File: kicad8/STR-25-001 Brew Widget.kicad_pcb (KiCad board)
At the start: 2 copper layers, 0 parts

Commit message: Started PCB Layout
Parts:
- added BT1: 18650, Battery:BatteryHolder_Keystone_1042_1x18650, B.Cu at (144.5, 114.9)
- added C1: 100nF, JLCPCB-Kicad-Footprints:C_0402, F.Cu at (153.3, 83.5)
- added C10: 100nF, JLCPCB-Kicad-Footprints:C_0402, F.Cu at (144.5, 117.8)
- added C11: 100nF, JLCPCB-Kicad-Footprints:C_0402, F.Cu at (147.0, 116.0)
- added C12: 10uF, JLCPCB-Kicad-Footprints:C_0402, F.Cu at (141.1, 107.0)
- added C13: 1uF, JLCPCB-Kicad-Footprints:C_0402, F.Cu at (118.0, 114.5)
- added C14: 100nF, JLCPCB-Kicad-Footprints:C_0402, F.Cu at (149.4, 108.8)
- added C15: 100nF, JLCPCB-Kicad-Footprints:C_0402, F.Cu at (152.4, 147.5)
- added C2: 4.7uF, JLCPCB-Kicad-Footprints:C_0402, F.Cu at (139.8, 82.5)
- added C3: 100nF, JLCPCB-Kicad-Footprints:C_0402, F.Cu at (139.8, 83.5)
- added C4: 100nF, JLCPCB-Kicad-Footprints:C_0402, F.Cu at (140.2, 77.8)
- added C5: 10uF, JLCPCB-Kicad-Footprints:C_0402, F.Cu at (139.2, 77.8)
- added C6: 10uF, JLCPCB-Kicad-Footprints:C_0402, F.Cu at (143.5, 117.8)
- added C7: 4.7uF, JLCPCB-Kicad-Footprints:C_0402, F.Cu at (120.4, 121.2)
- added C8: 4.7uF, JLCPCB-Kicad-Footprints:C_0402, F.Cu at (145.9, 105.8)
- added C9: 10pF, JLCPCB-Kicad-Footprints:C_0402, F.Cu at (118.0, 112.7)
- added D1: B16WS, JLCPCB-Kicad-Footprints:D_SOD-323, F.Cu at (113.7, 113.0)
- added D2: Red, LED_SMD:LED_0603_1608Metric, F.Cu at (141.7, 101.0)
- added D3: Green, LED_SMD:LED_0603_1608Metric, F.Cu at (144.0, 101.0)
- added D4: B16WS, JLCPCB-Kicad-Footprints:D_SOD-323, F.Cu at (137.5, 120.2)
- added H1: ~, JLCPCB-Kicad-Footprints:Hole_Tooling_JLCPCB, F.Cu at (178.3, 116.8)
- added H2: ~, JLCPCB-Kicad-Footprints:Hole_Tooling_JLCPCB, F.Cu at (178.3, 119.8)
- added H3: ~, JLCPCB-Kicad-Footprints:Hole_Tooling_JLCPCB, F.Cu at (178.3, 122.8)
- added J1: USB_B_Micro, STR-USB:USB_Micro-B_C319160, F.Cu at (136.2, 73.6)
- added L1: 10uH,600mA, Inductor_SMD:L_Wuerth_WE-GF-1210, F.Cu at (137.2, 117.0)
- added PN1: ~, JLCPCB-Kicad-Footprints:Part_Num_JLCPCB, F.Cu at (181.5, 114.5)
- added Q1: IRLML6401, Package_TO_SOT_SMD:SOT-23, F.Cu at (137.1, 108.7)
- added Q2: FS8205A, Package_TO_SOT_SMD:SOT-23-6, F.Cu at (145.5, 148.0)
- added R1: 10kΩ, JLCPCB-Kicad-Footprints:R_0402, F.Cu at (139.8, 79.2)
- added R10: 2kΩ, JLCPCB-Kicad-Footprints:R_0402, F.Cu at (145.9, 103.9)
- added R11: 200kΩ, JLCPCB-Kicad-Footprints:R_0402, F.Cu at (118.0, 120.1)
- added R12: 120kΩ, JLCPCB-Kicad-Footprints:R_0402, F.Cu at (118.0, 121.9)
- added R13: 4.7kΩ, JLCPCB-Kicad-Footprints:R_0402, F.Cu at (144.3, 158.2)
- added R14: 100Ω, JLCPCB-Kicad-Footprints:R_0402, F.Cu at (153.4, 147.5)
- added R15: 0Ω, JLCPCB-Kicad-Footprints:R_0402, F.Cu at (141.9, 148.9)
- added R16: 1kΩ, JLCPCB-Kicad-Footprints:R_0402, F.Cu at (148.7, 150.3)
- added R17: 10kΩ, JLCPCB-Kicad-Footprints:R_0402, F.Cu at (153.0, 110.3)
- added R2: 10kΩ, JLCPCB-Kicad-Footprints:R_0402, F.Cu at (153.3, 84.5)
- added R3: 10kΩ, JLCPCB-Kicad-Footprints:R_0402, F.Cu at (139.8, 81.5)
- added R4: 10kΩ, JLCPCB-Kicad-Footprints:R_0402, F.Cu at (139.8, 84.4)
- added R5: 4.7kΩ, JLCPCB-Kicad-Footprints:R_0402, F.Cu at (143.9, 111.2)
- added R6: 4.7kΩ, JLCPCB-Kicad-Footprints:R_0402, F.Cu at (141.9, 111.2)
- added R7: 10kΩ, JLCPCB-Kicad-Footprints:R_0402, F.Cu at (151.2, 83.5)
- added R8: 100kΩ, JLCPCB-Kicad-Footprints:R_0402, F.Cu at (118.0, 118.2)
- added R9: 2kΩ, JLCPCB-Kicad-Footprints:R_0402, F.Cu at (142.8, 98.7)
- added SW1: SW_MINI, STR-Switch:SW_SMD_SPST_8x3.6, F.Cu at (147.5, 90.2)
- added SW2: SW_MINI, STR-Switch:SW_SMD_SPST_8x3.6, F.Cu at (141.2, 90.2)
- added U1: ESP32-C3-MINI-1-N4, STR-ESP32:ESP32-C3-MINI-1-N4, F.Cu at (148.7, 74.0)
- added U2: TPS61040, JLCPCB-Kicad-Footprints:SOT-23-5_L3.0-W1.7-P0.95-LS2.8-BL, F.Cu at (123.0, 118.5)
- added U3: TP4057, Package_TO_SOT_SMD:TSOT-23-6, F.Cu at (142.8, 104.9)
- added U4: MPU-6500, Sensor_Motion:InvenSense_QFN-24_3x3mm_P0.4mm_NoMask, F.Cu at (144.2, 114.5)
- added U5: DS18B20U, Package_SO:MSOP-8_3x3mm_P0.65mm, F.Cu at (144.5, 160.5)
- added U6: MAX17048, Package_DFN_QFN:TDFN-8-1EP_2x2mm_P0.5mm_EP0.8x1.2mm, F.Cu at (151.5, 108.5)
- added U7: DW01A, Package_TO_SOT_SMD:SOT-23-6, F.Cu at (149.8, 147.9)
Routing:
- net +BATT: track 0.00 -> 93.4 mm, vias 0 -> 4
- net GND: track 0.00 -> 78.8 mm, vias 0 -> 29
- net -BATT: track 0.00 -> 55.4 mm
- net USB_D+: track 0.00 -> 47.9 mm
- net USB_D-: track 0.00 -> 45.6 mm
- net SCA: track 0.00 -> 38.1 mm, vias 0 -> 2
- net VBUS: track 0.00 -> 35.8 mm, vias 0 -> 4
- net SCL: track 0.00 -> 32.7 mm, vias 0 -> 1
- net +3.3V: track 0.00 -> 29.7 mm, vias 0 -> 11
- net /-BATT_NOPROT: track 0.00 -> 22.1 mm, vias 0 -> 3
- net EN: track 0.00 -> 9.87 mm
- net GPIO9: track 0.00 -> 8.95 mm
- net ~{BAT_ALERT}: track 0.00 -> 7.37 mm
- net Net-(U1-IO2): track 0.00 -> 4.95 mm
- net Net-(D3-K): track 0.00 -> 4.93 mm
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- added copper zone on In1.Cu, net +3.3V
- added copper zone on In2.Cu, net GND
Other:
- board outline added: 25 x 94 mm
- copper layers 2 -> 4

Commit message: PCB routed and all 3d models correct, needs final review
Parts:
- removed the C13 at (118.0, 114.5)
- removed H1, H2, H3: ~, JLCPCB-Kicad-Footprints:Hole_Tooling_JLCPCB
- removed the U2 at (123.0, 118.5)
- added C10: 100pF, JLCPCB-Kicad-Footprints:C_0402, F.Cu at (141.8, 116.9)
- added C16: 100pF, JLCPCB-Kicad-Footprints:C_0402, F.Cu at (137.3, 126.5)
- added C17: 1uF, JLCPCB-Kicad-Footprints:C_0402, F.Cu at (137.3, 127.4)
- added C18: 10uF, JLCPCB-Kicad-Footprints:C_0402, F.Cu at (137.3, 128.3)
- added C19: 10uF, JLCPCB-Kicad-Footprints:C_0402, F.Cu at (137.3, 129.2)
- added C8: 10uF, JLCPCB-Kicad-Footprints:C_0402, F.Cu at (141.8, 115.1)
- added C9: 1uF, JLCPCB-Kicad-Footprints:C_0402, F.Cu at (141.8, 116.0)
- added TP1: TestPoint, TestPoint:TestPoint_Pad_D2.0mm, F.Cu at (134.6, 84.0)
- added TP10: TestPoint, TestPoint:TestPoint_Pad_D1.0mm, F.Cu at (133.9, 77.3)
- added TP11: TestPoint, TestPoint:TestPoint_Pad_D1.0mm, F.Cu at (133.9, 79.5)
- added TP2: TestPoint, TestPoint:TestPoint_Pad_D2.0mm, F.Cu at (136.3, 114.0)
- added TP3: TestPoint, TestPoint:TestPoint_Pad_D2.0mm, F.Cu at (136.4, 134.6)
- added TP4: TestPoint, TestPoint:TestPoint_Pad_D2.0mm, F.Cu at (151.8, 142.3)
- added TP5: TestPoint, TestPoint:TestPoint_Pad_D2.0mm, F.Cu at (153.5, 104.3)
- added TP6: TestPoint, TestPoint:TestPoint_Pad_D2.0mm, F.Cu at (141.3, 97.7)
- added TP7: TestPoint, TestPoint:TestPoint_Pad_D2.0mm, F.Cu at (147.3, 97.8)
- added TP8: TestPoint, TestPoint:TestPoint_Pad_D2.0mm, F.Cu at (145.1, 142.2)
- added TP9: TestPoint, TestPoint:TestPoint_Pad_2.5x2.5mm, F.Cu at (151.8, 133.3)
- added U3: MT3608, Package_TO_SOT_SMD:SOT-23-6, F.Cu at (140.3, 119.7)
- C7: value 4.7uF -> 10uF
- D2: value Red -> CHG
- D3: value Green -> STBY
- J1: footprint STR-USB:USB_Micro-B_C319160 -> Connector_USB:USB_Micro-B_Molex_47346-0001
- L1: value 10uH,600mA -> 22uH,540mA; footprint Inductor_SMD:L_Wuerth_WE-GF-1210 -> STR-Passive:IND_LQH3NPZ220MMEL
- R11: value 200kΩ -> 68kΩ
- R12: value 120kΩ -> 15kΩ
- SW1: value SW_MINI -> BOOT
- SW2: value SW_MINI -> RESET
- moved PN1 47.5 mm to (148.5, 80.3)
- moved C13 26.0 mm to (141.4, 124.1), turned to 90 degrees
- moved R11 24.7 mm to (142.4, 124.1), turned to 90 degrees
- moved R12 22.9 mm to (140.9, 122.6), turned to 180 degrees
- moved C7 22.6 mm to (141.8, 114.1), turned to 0 degrees
- moved D1 21.8 mm to (135.2, 109.5), turned to 90 degrees
- moved R8 18.2 mm to (133.7, 109.0), turned to -90 degrees
- moved C15 10.0 mm to (136.5, 98.1)
- moved D3 9.49 mm to (134.6, 102.0), turned to 180 degrees
- moved C11 8.79 mm to (137.6, 103.1)
- moved R9 8.78 mm to (134.2, 97.1)
- moved D2 7.29 mm to (134.5, 99.4), turned to 180 degrees
- moved R5 7.08 mm to (144.6, 104.1)
- moved R6 7.08 mm to (142.6, 104.1)
- moved C12 7.04 mm to (145.2, 110.7)
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- renumbered C8 to C11, C10 to C12, C9 to C13, C11 to C14, C12 to C15, C14 to C20, C15 to C21, R14 to R13, R13 to R14, R17 to R15, R15 to R16, R16 to R17, U3 to U2, U6 to U5, U5 to U6
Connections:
- net Net-(Q1-S) renamed /VIN
- net Net-(U2-FB) renamed /FB
- net Net-(U2-SW) renamed /VOUT
- R6 pad 2: SCA -> SDA
- U1 pad 6: SCA -> SDA
- U4 pad 24: SCA -> SDA
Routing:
- net TEMP: track 2.66 -> 94.2 mm
- net SDA: track 0.00 -> 50.7 mm, vias 0 -> 2
- net SCA: track 38.1 -> 0.00 mm, vias 2 -> 0
- net ~{BAT_ALERT}: track 7.37 -> 38.1 mm
- net USB_D+: track 47.9 -> 27.3 mm, vias 0 -> 2
- net USB_D-: track 45.6 -> 27.9 mm, vias 0 -> 2
- net +3.3V: track 29.7 -> 46.3 mm, vias 11 -> 21
- net VBUS: track 35.8 -> 49.5 mm, vias 4 -> 6
- net SCL: track 32.7 -> 45.3 mm, vias 1 -> 4
- net /VIN: track 0.00 -> 12.4 mm
- net GND: track 78.8 -> 91.0 mm, vias 29 -> 40
- net +BATT: track 93.4 -> 103.6 mm, vias 4 -> 5
- net EN: track 9.87 -> 18.3 mm
- net -BATT: track 55.4 -> 50.5 mm
- net /FB: track 0.00 -> 3.79 mm
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- added copper zone on F.Cu, net +3.3V
- added copper zone on F.Cu, net /VIN
- added copper zone on F.Cu, net /VOUT
- added copper zone on F.Cu, net GND
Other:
- board text added: "+"
- board text added: "+3.3v"
- board text added: "-"
- board text added: "BOOT"
- board text added: "Brew Widget"
- board text added: "CHG"
- board text added: "GND"
- board text added: "RESET"
- board text added: "STBY"
- board text added: "STR-25-001 REVA"
- board text added: "X"
- board text added: "Y"

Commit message: Added TP labels on top silkscreen
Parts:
- moved TP4 1.22 mm to (151.8, 141.1)
- moved TP8 1.16 mm to (145.2, 141.1)
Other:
- board text added: "+BAT"
- board text added: "-BAT"
- board text added: "SCL"
- board text added: "SDA"
- board text added: "TEMP"
- board text added: "VBUS"
- board text added: "VIN"

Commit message: Fix DRC
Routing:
- net +BATT: track 103.6 -> 105.2 mm
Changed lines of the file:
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@@
 	)
 	(gr_text "CHG"
-		(at 132.88 101.11 0)
+		(at 132.86 101.17 0)
 		(layer "F.SilkS")
 		(effects
@@
 	)
 	(gr_text "STBY"
-		(at 132.92 103.76 0)
+		(at 132.93 103.91 0)
 		(layer "F.SilkS")
 		(effects
@@
 	)
 	(segment
-		(start 143.05 148.9375)
-		(end 143.05 142.21)
-		(width 0.3)
-		(layer "F.Cu")
-		(net 2)
-	)
-	(segment
 		(start 148.66 114.059999)
 		(end 148.66 113.91)
@@
 	)
 	(segment
+		(start 143.05 141.18)
+		(end 143.05 141)
+		(width 0.3)
+		(layer "F.Cu")
+		(net 2)
+	)
+	(segment
 		(start 144.92 126.7)
 		(end 144.92 116.34)
@@
 	)
 	(segment
-		(start 145.18 141.08)
-		(end 143.13 141.08)
-		(width 0.3)
-		(layer "F.Cu")
-		(net 2)
-	)
-	(segment
 		(start 146.1725 115.0875)
 		(end 146.1725 114.46)
@@
 	)
 	(segment
-		(start 143.08 142.24)
-		(end 143.05 142.21)
-		(width 0.2)
-		(layer "F.Cu")
-		(net 2)
-	)
-	(segment
 		(start 148.66 113.760001)
 		(end 148.66 113.91)
@@
 	)
 	(segment
+		(start 145.18 141.08)
+		(end 143.15 141.08)
+		(width 0.3)
+		(layer "F.Cu")
+		(net 2)
+	)
+	(segment
 		(start 147.6725 113.16)
 		(end 148.059999 113.16)
@@
 	)
 	(segment
+		(start 143.15 141.08)
+		(end 143.05 141.18)
+		(width 0.3)
+		(layer "F.Cu")
+		(net 2)
+	)
+	(segment
 		(start 143.05 128.57)
 		(end 144.92 126.7)
@@
 	)
 	(segment
+		(start 143.05 148.9375)
+		(end 143.05 141.18)
+		(width 0.3)
+		(layer "F.Cu")
+		(net 2)
+	)
+	(segment
 		(start 144.3625 148.9375)
 		(end 143.05 148.9375)
@@
 	)
 	(segment
-		(start 143.05 142.21)
-		(end 143.05 141)
-		(width 0.3)
-		(layer "F.Cu")
-		(net 2)
-	)
-	(segment
 		(start 148.059999 114.66)
 		(end 148.66 114.059999)
 		(width 0.2)
-		(layer "F.Cu")
-		(net 2)
-	)
-	(segment
-		(start 143.13 141.08)
-		(end 143.05 141)
-		(width 0.3)
 		(layer "F.Cu")
 		(net 2)
@@
 	)
 	(segment
+		(start 151.82 144.52)
+		(end 151.82 141.08)
+		(width 0.2)
+		(layer "F.Cu")
+		(net 7)
+	)
+	(segment
 		(start 140.0175 108.7)
 		(end 140.0175 107.5225)
@@
 	)
 	(segment
-		(start 151.82 144.52)
-		(end 153.3625 146.0625)
+		(start 153.3625 146.0625)
+		(end 151.82 144.52)
 		(width 0.2)
 		(layer "F.Cu")
@@
 		(layer "F.Cu")
 		(net 7)
-	)
-	(segment
-		(start 151.82 142.61)
-		(end 151.82 144.52)
-		(width 0.2)
-		(layer "F.Cu")
-		(net 7)

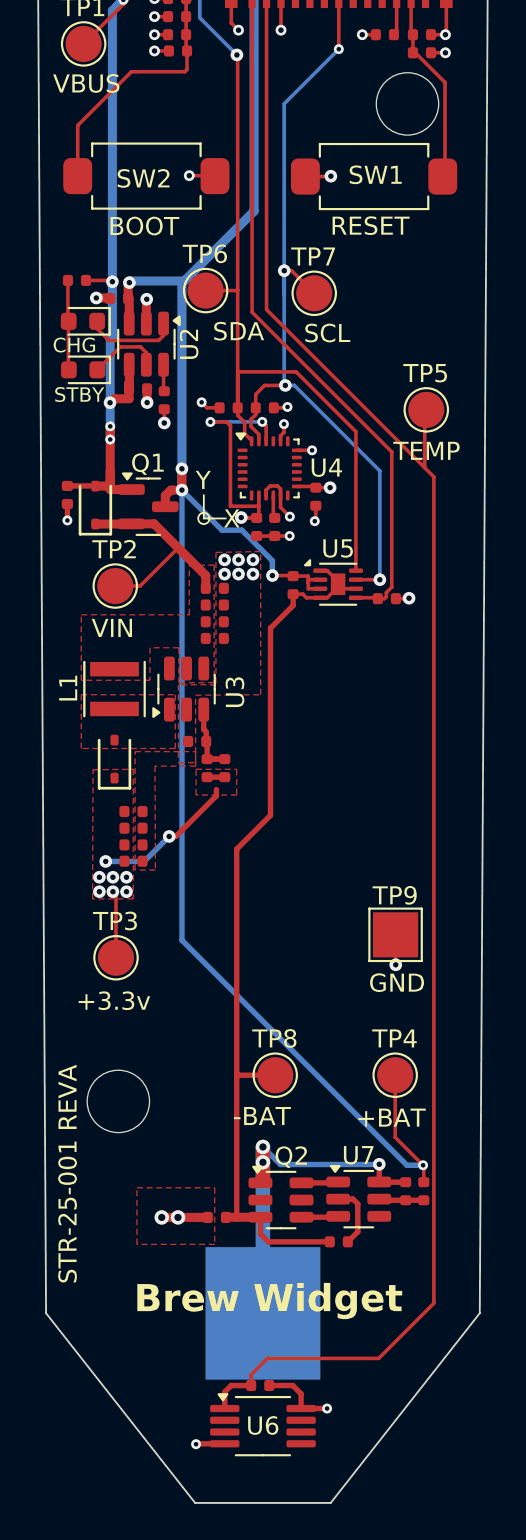
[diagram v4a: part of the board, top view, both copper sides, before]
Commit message: Added Fiducals
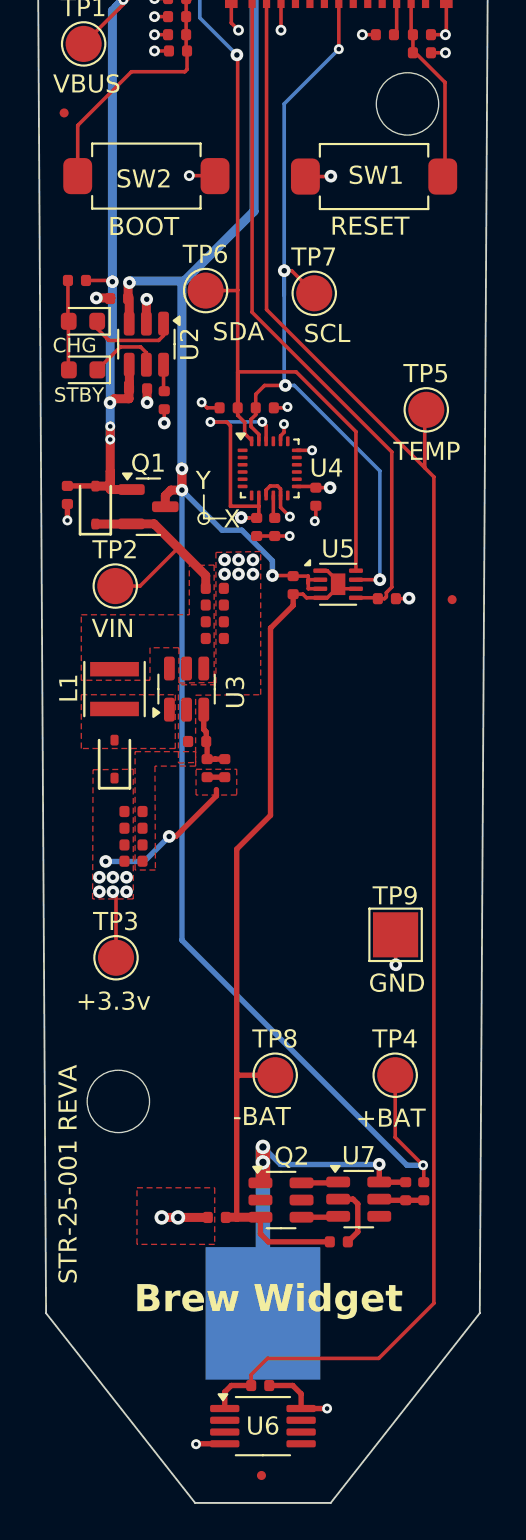
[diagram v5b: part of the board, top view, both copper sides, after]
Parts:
- added FID1: Fiducial, Fiducial:Fiducial_0.5mm_Mask1mm, F.Cu at (133.5, 87.8)
- added FID2: Fiducial, Fiducial:Fiducial_0.5mm_Mask1mm, F.Cu at (155.0, 114.8)
- added FID3: Fiducial, Fiducial:Fiducial_0.5mm_Mask1mm, F.Cu at (144.4, 163.2)
